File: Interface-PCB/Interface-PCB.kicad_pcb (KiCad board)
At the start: 2 copper layers, 85.1 x 73.7 mm, 65 parts, among them IC1 SN74LVC245AN, IC2 TBD62783A, IC3 TBD62783A, J1 BARREL_JACK_PAD, J10 LEVEL_SENSOR, J11 LEVEL_SENSOR, J12 TEMPERATURE_SENSOR, J13 TEMPERATURE_SENSOR, J14 CONN_05JST, J15 CONN_05JST, J2 BARREL_JACK_PAD, J3 GPIO_DEBUG_HEADER, J4 RASPBERRYPI_GPIO_CONN_HEADER, J5 I2C_HEADER, J6 LEVEL_SENSOR, J7 LEVEL_SENSOR, J8 LEVEL_SENSOR, J9 LEVEL_SENSOR, M1 PERISTALTIC_PUMP, M2 PERISTALTIC_PUMP, M3 PERISTALTIC_PUMP, U1 TB6612FNG_BREAKOUT, U2 TB6612FNG_BREAKOUT, U3 CD74HC4067_MUX

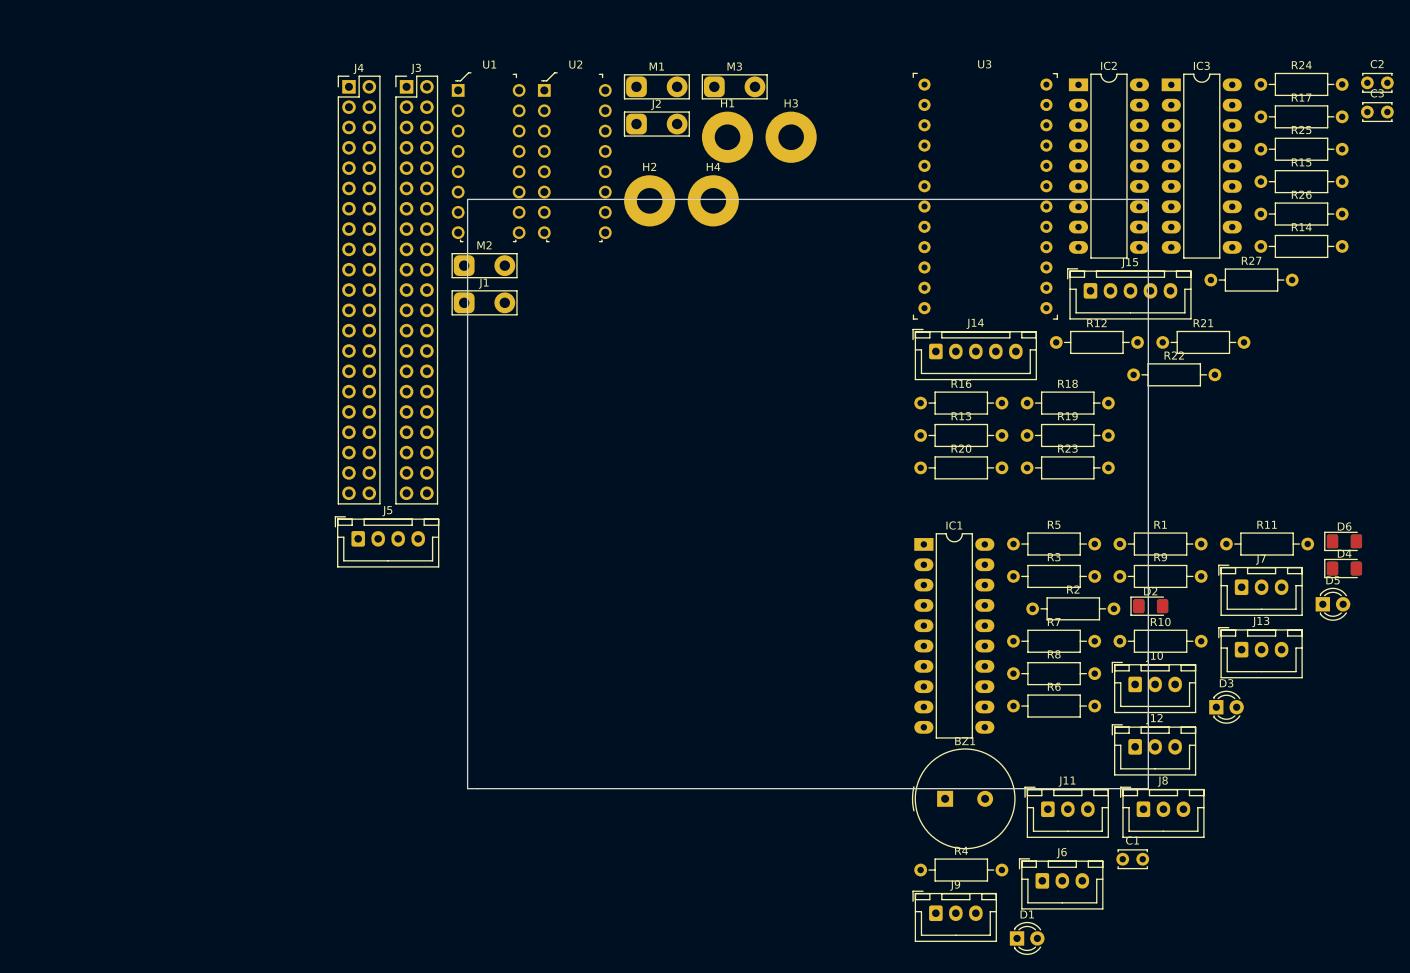
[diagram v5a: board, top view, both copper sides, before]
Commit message: Setup JLCPCB Plotting Rules
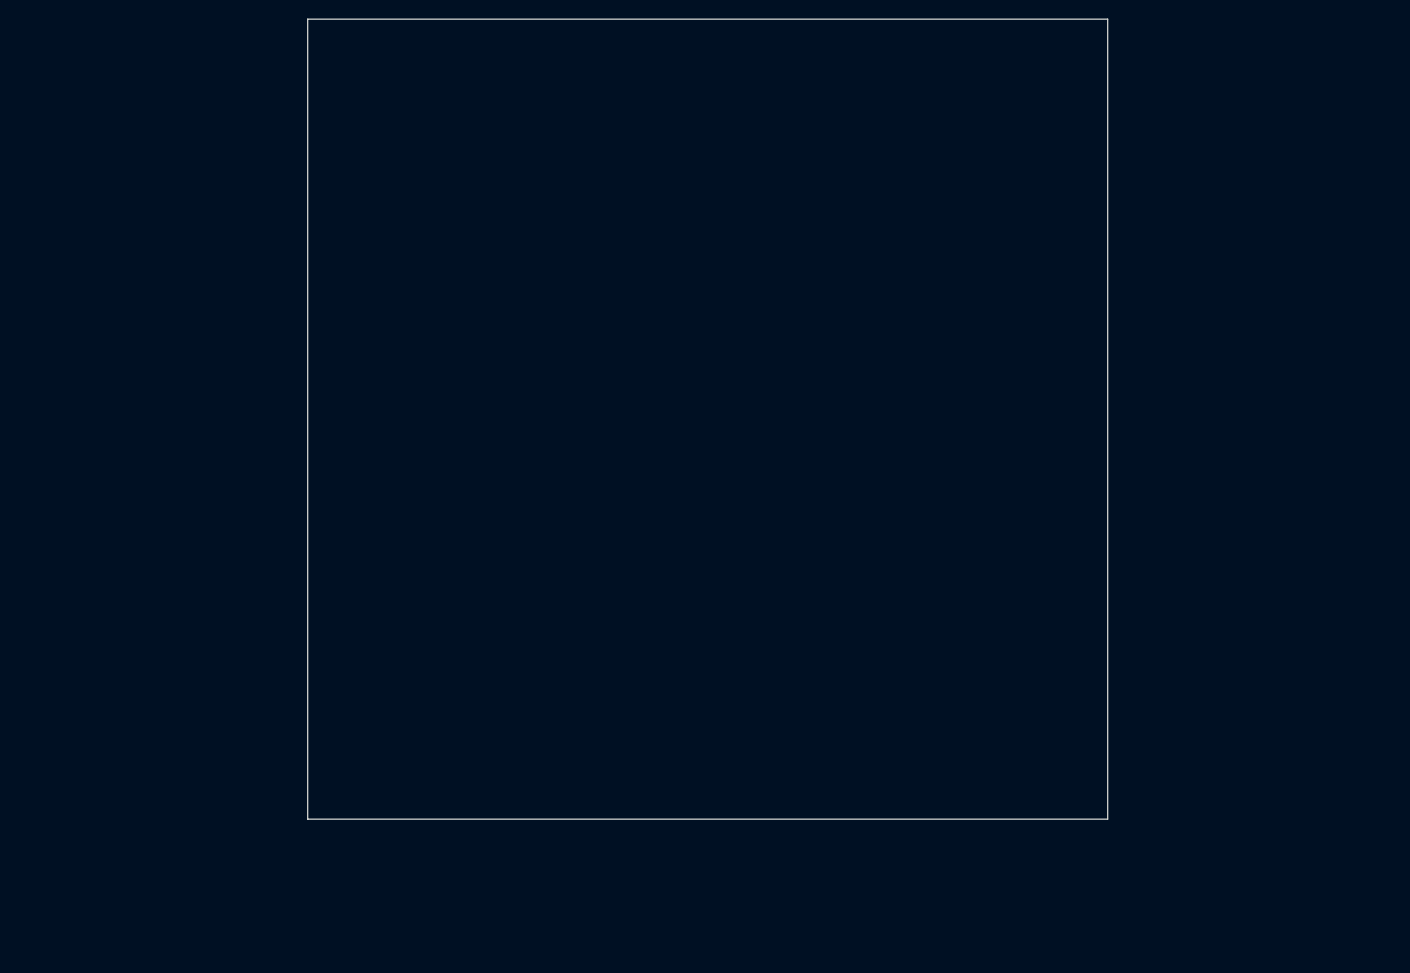
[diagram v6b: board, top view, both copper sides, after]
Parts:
- removed BZ1: Buzzer, Buzzer_Beeper:Buzzer_TDK_PS1240P02BT_D12.2mm_H6.5mm
- removed C1, C2, C3: 100nF, Capacitor_THT:C_Disc_D3.4mm_W2.1mm_P2.50mm
- removed D1: 12V_ON, LED_THT:LED_D3.0mm
- removed D2: 12V_ON_SMD, LED_SMD:LED_1206_3216Metric_Pad1.42x1.75mm_HandSolder
- removed D3: USER_LED, LED_THT:LED_D3.0mm
- removed D4: USER_LED_SMD, LED_SMD:LED_1206_3216Metric_Pad1.42x1.75mm_HandSolder
- removed D5: 5V_ON, LED_THT:LED_D3.0mm
- removed D6: 5V_ON_SMD, LED_SMD:LED_1206_3216Metric_Pad1.42x1.75mm_HandSolder
- removed H1, H2, H3, H4: MountingHole, MountingHole:MountingHole_3.2mm_M3_Pad
- removed IC1: SN74LVC245AN, Package_DIP:DIP-20_W7.62mm_LongPads
- removed IC2, IC3: TBD62783A, Package_DIP:DIP-18_W7.62mm_LongPads
- removed J1, J2: BARREL_JACK_PAD, TestPoint:TestPoint_2Pads_Pitch5.08mm_Drill1.3mm
- removed J10, J11, J6, J7, J8, J9: LEVEL_SENSOR, Connector_JST:JST_XH_B3B-XH-A_1x03_P2.50mm_Vertical
- removed J12, J13: TEMPERATURE_SENSOR, Connector_JST:JST_XH_B3B-XH-A_1x03_P2.50mm_Vertical
- removed J14, J15: CONN_05JST, Connector_JST:JST_XH_B5B-XH-A_1x05_P2.50mm_Vertical
- removed J3: GPIO_DEBUG_HEADER, Connector_PinHeader_2.54mm:PinHeader_2x21_P2.54mm_Vertical
- removed J4: RASPBERRYPI_GPIO_CONN_HEADER, Connector_PinHeader_2.54mm:PinHeader_2x21_P2.54mm_Vertical
- removed J5: I2C_HEADER, Connector_JST:JST_XH_B4B-XH-A_1x04_P2.50mm_Vertical
- removed M1, M2, M3: PERISTALTIC_PUMP, TestPoint:TestPoint_2Pads_Pitch5.08mm_Drill1.3mm
- removed R1: 680, Resistor_THT:R_Axial_DIN0207_L6.3mm_D2.5mm_P10.16mm_Horizontal
- removed R10, R11, R6, R7, R8, R9: 220, Resistor_THT:R_Axial_DIN0207_L6.3mm_D2.5mm_P10.16mm_Horizontal
- removed R12, R13, R14, R15, R16, R17, R18, R19, R20, R21, R22, R23, R24, R25, R26, R27, R4, R5: 10k, Resistor_THT:R_Axial_DIN0207_L6.3mm_D2.5mm_P10.16mm_Horizontal
- removed R2: 100, Resistor_THT:R_Axial_DIN0207_L6.3mm_D2.5mm_P10.16mm_Horizontal
- removed R3: 200, Resistor_THT:R_Axial_DIN0207_L6.3mm_D2.5mm_P10.16mm_Horizontal
- removed U1, U2: TB6612FNG_BREAKOUT, digikey-footprints:DIP-16_W7.62mm
- removed U3: CD74HC4067_MUX, digikey-footprints:Socket_DIP-24_15.24mm_Conn
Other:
- board size 85.1 x 73.7 mm -> 100 x 100 mm

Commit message: Add JLC design rules
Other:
- rule pad_to_mask_clearance: 0 -> 0.05
- board text added: "0.1270 mm / 0.1270 mm"
- board text added: "0.2000 mm"
- board text added: "1.6000 mm"
- board text added: "100.0500 mm x 100.0500 mm"
- board text added: "2"
- board text added: "BOARD CHARACTERISTICS"
- board text added: "Board Thickness:"
- board text added: "Board overall dimensions:"
- board text added: "Castellated pads:"
- board text added: "Copper Finish:"
- board text added: "Copper Layer Count:"
- board text added: "Edge card connectors:"
- board text added: "HAL SnPb"
- board text added: "Impedance Control:"
- board text added: "Min hole diameter:"
- board text added: "Min track/spacing:"
- board text added: "No"
- board text added: "Plated Board Edge:"
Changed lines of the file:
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@@
       (layer "B.Paste" (type "Bottom Solder Paste"))
       (layer "B.SilkS" (type "Bottom Silk Screen") (color "White"))
-      (copper_finish "None")
+      (copper_finish "HAL SnPb")
       (dielectric_constraints no)
     )
-    (pad_to_mask_clearance 0)
+    (pad_to_mask_clearance 0.05)
+    (solder_mask_min_width 0.2)
     (pcbplotparams
       (layerselection 0x00010fc_ffffffff)
@@
   (net 0 "")
   (gr_rect (start 100.66 49.86) (end 200.66 149.86) (layer "Edge.Cuts") (width 0.05) (fill none))
+  (gr_text "Min hole diameter: " (at 166.221429 29) (layer "Cmts.User")
+    (effects (font (size 1.5 1.5) (thickness 0.2)) (justify left top))
+  )
+  (gr_text "" (at 191.064286 24.785) (layer "Cmts.User")
+    (effects (font (size 1.5 1.5) (thickness 0.2)) (justify left top))
+  )
+  (gr_text "BOARD CHARACTERISTICS" (at 96 15) (layer "Cmts.User")
+    (effects (font (size 2 2) (thickness 0.4)) (justify left top))
+  )
+  (gr_text "2" (at 129.307143 20.57) (layer "Cmts.User")
+    (effects (font (size 1.5 1.5) (thickness 0.2)) (justify left top))
+  )
+  (gr_text "Edge card connectors: " (at 96.75 41.645) (layer "Cmts.User")
+    (effects (font (size 1.5 1.5) (thickness 0.2)) (justify left top))
+  )
+  (gr_text "No" (at 129.307143 41.645) (layer "Cmts.User")
+    (effects (font (size 1.5 1.5) (thickness 0.2)) (justify left top))
+  )
+  (gr_text "No" (at 129.307143 37.43) (layer "Cmts.User")
+    (effects (font (size 1.5 1.5) (thickness 0.2)) (justify left top))
+  )
+  (gr_text "No" (at 191.064286 33.215) (layer "Cmts.User")
+    (effects (font (size 1.5 1.5) (thickness 0.2)) (justify left top))
+  )
+  (gr_text "Min track/spacing: " (at 96.75 29) (layer "Cmts.User")
+    (effects (font (size 1.5 1.5) (thickness 0.2)) (justify left top))
+  )
+  (gr_text "0.1270 mm / 0.1270 mm" (at 129.307143 29) (layer "Cmts.User")
+    (effects (font (size 1.5 1.5) (thickness 0.2)) (justify left top))
+  )
+  (gr_text "HAL SnPb" (at 129.307143 33.215) (layer "Cmts.User")
+    (effects (font (size 1.5 1.5) (thickness 0.2)) (justify left top))
+  )
+  (gr_text "Board overall dimensions: " (at 96.75 24.785) (layer "Cmts.User")
+    (effects (font (size 1.5 1.5) (thickness 0.2)) (justify left top))
+  )
+  (gr_text "Impedance Control: " (at 166.221429 33.215) (layer "Cmts.User")
+    (effects (font (size 1.5 1.5) (thickness 0.2)) (justify left top))
+  )
+  (gr_text "Copper Layer Count: " (at 96.75 20.57) (layer "Cmts.User")
+    (effects (font (size 1.5 1.5) (thickness 0.2)) (justify left top))
+  )
+  (gr_text "100.0500 mm x 100.0500 mm" (at 129.307143 24.785) (layer "Cmts.User")
+    (effects (font (size 1.5 1.5) (thickness 0.2)) (justify left top))
+  )
+  (gr_text "0.2000 mm" (at 191.064286 29) (layer "Cmts.User")
+    (effects (font (size 1.5 1.5) (thickness 0.2)) (justify left top))
+  )
+  (gr_text "Board Thickness: " (at 166.221429 20.57) (layer "Cmts.User")
+    (effects (font (size 1.5 1.5) (thickness 0.2)) (justify left top))
+  )
+  (gr_text "Copper Finish: " (at 96.75 33.215) (layer "Cmts.User")
+    (effects (font (size 1.5 1.5) (thickness 0.2)) (justify left top))
+  )
+  (gr_text "" (at 166.221429 24.785) (layer "Cmts.User")
+    (effects (font (size 1.5 1.5) (thickness 0.2)) (justify left top))
+  )
+  (gr_text "1.6000 mm" (at 191.064286 20.57) (layer "Cmts.User")
+    (effects (font (size 1.5 1.5) (thickness 0.2)) (justify left top))
+  )
+  (gr_text "No" (at 191.064286 37.43) (layer "Cmts.User")
+    (effects (font (size 1.5 1.5) (thickness 0.2)) (justify left top))
+  )
+  (gr_text "Castellated pads: " (at 96.75 37.43) (layer "Cmts.User")
+    (effects (font (size 1.5 1.5) (thickness 0.2)) (justify left top))
+  )
+  (gr_text "Plated Board Edge: " (at 166.221429 37.43) (layer "Cmts.User")
+    (effects (font (size 1.5 1.5) (thickness 0.2)) (justify left top))
+  )
+  (group "group-boardCharacteristics" (id c0acfb15-02d9-42a3-a500-96274a64592b)
+    (members
+      14e5ac74-9e6a-429c-a85f-3f85c24f6634
+      20a5fa03-1925-401c-ab1e-0afe600eece7
+      210b172c-b965-4a60-99f4-39f3cf0b0a90
+      23d6215c-5ccd-448a-9dca-fb24b263b819
+      2501f8af-64a4-4048-910a-af6739d92186
+      2887f18d-0aa0-4560-89a5-469e7311c504
+      2dc8128f-408c-4d56-91b5-3b4d4c6dd33f
+      32ad7fbe-e026-4d57-9f6b-f4af30c894d9
+      4833e46b-f647-4405-8958-8388c09e9ad1
+      4b49296e-e16b-4f09-89ae-9e00f97c6e61
+      524a8897-4b26-49dd-b508-9c5b2f671e31
+      623f0fd1-05e3-4aed-b4a4-842ebc101656
+      72c8bab7-3236-4d5e-a06f-9f8b3d4cd3c8
+      75b6e061-3edd-496d-8819-9872e3fcd769
+      7ab43dd5-158c-4fb4-89fd-0268b2095c18
+      7db1c116-53cc-43a8-9a9d-fcc8da2afbb1
+      7ddaea75-0e14-403a-984d-c1eba0e6698b
+      931e27aa-b13d-4318-a4da-bc41de9026c2
+      af6768f8-3c5e-4c2e-ad12-97c0640b49b0
+      bdc2dce2-a873-4024-ba32-25e14d4c7d3a
+      bf3b8360-7021-4a05-9a17-ac671301ba24
+      fa3e4d8c-7c0c-49b2-8f34-dbc76c0c364e
+      febb7d9c-f8af-428a-b455-1415daa5c3f8
+    )
+  )
 )
